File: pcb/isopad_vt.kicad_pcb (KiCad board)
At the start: 2 copper layers, 26.2 x 35.7 mm, 2 parts, among them U1 RP2040_Zero

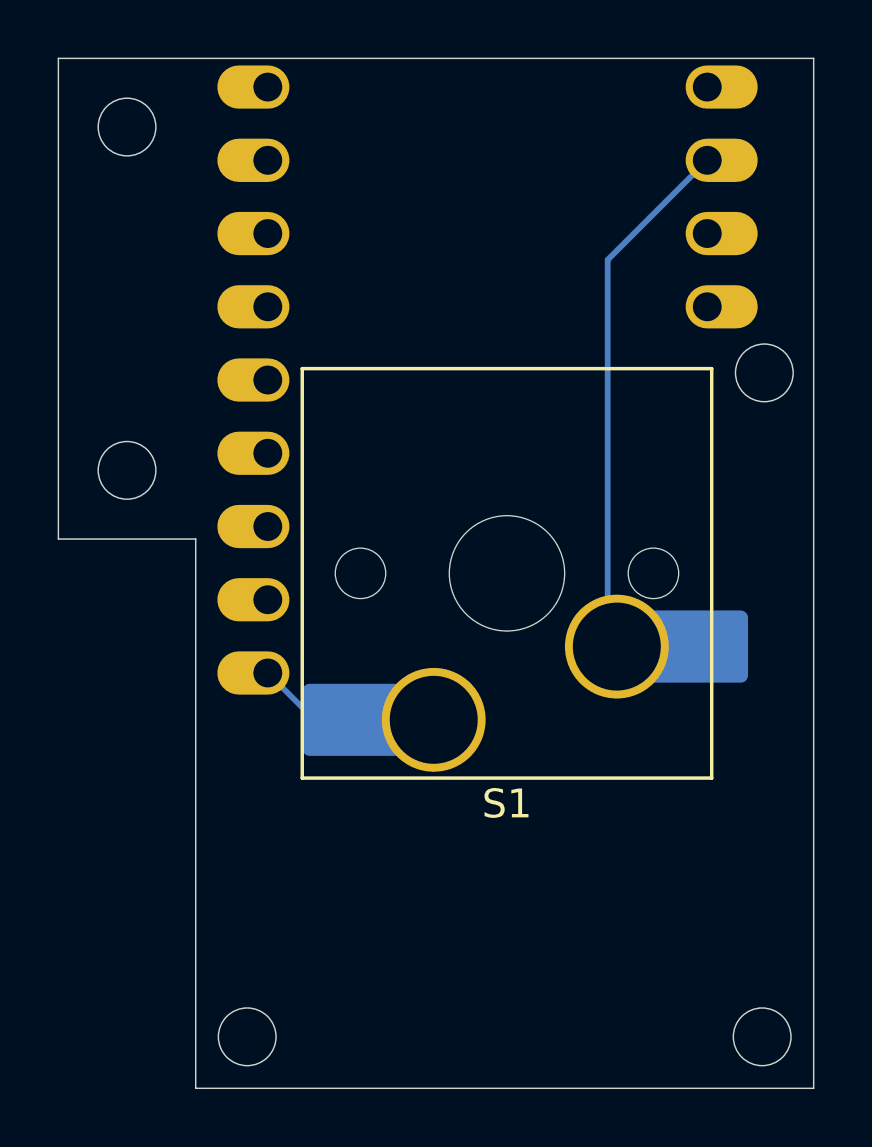
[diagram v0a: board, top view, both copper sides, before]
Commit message: case files and firmware
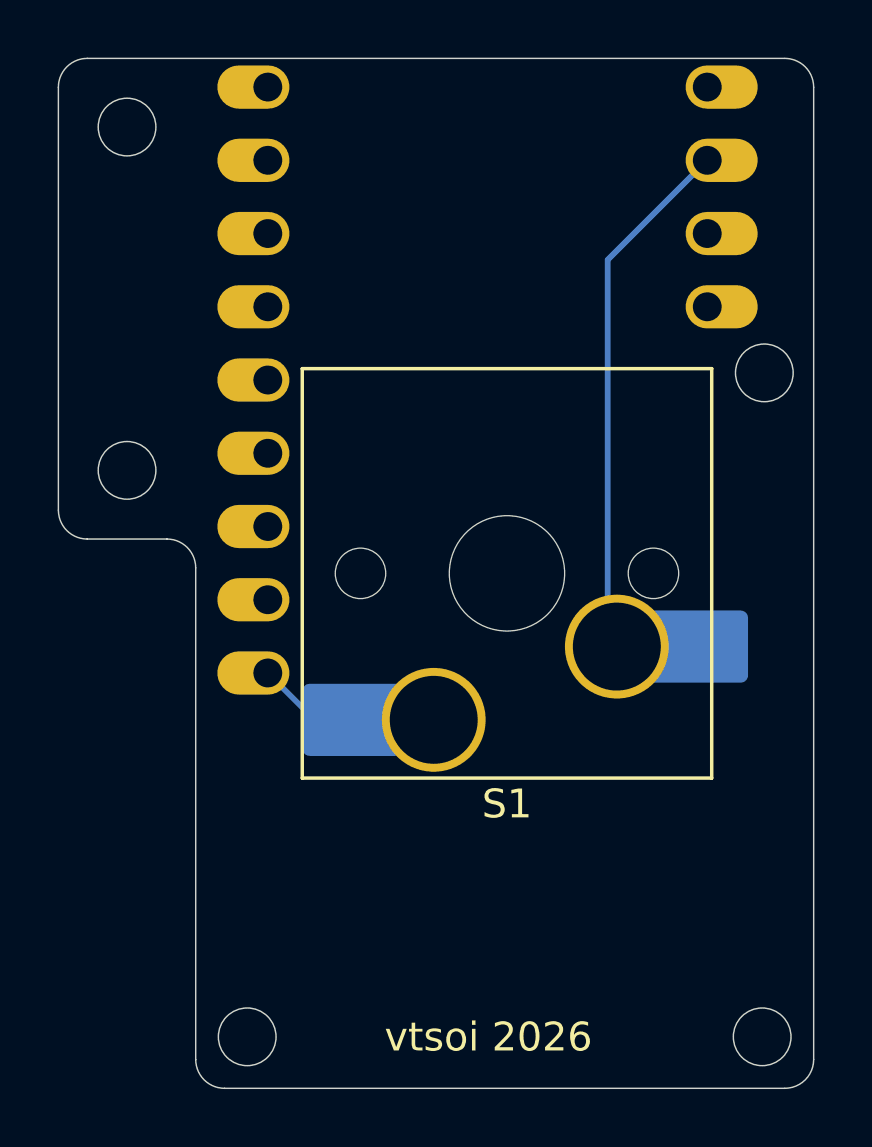
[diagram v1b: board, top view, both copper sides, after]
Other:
- outline, holes or cut-outs redrawn
- board text added: "vtsoi 2026"
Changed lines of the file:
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@@
 		(tags "Kailh Keyboard Keyswitch Switch Hotswap Socket Plated Relief Cutout Keycap ISOEnter 180deg")
 		(property "Reference" "S1"
-			(at 0 -8 360)
+			(at 0 -8 0)
 			(layer "F.SilkS")
 			(effects
@@
 		)
 		(property "Value" "Keyswitch"
-			(at 0 8 360)
+			(at 0 8 0)
 			(layer "F.Fab")
 			(effects
@@
 		)
 		(property "Footprint" "PCM_Switch_Keyboard_Hotswap_Kailh:SW_Hotswap_Kailh_MX_Plated_ISOEnter_180deg"
-			(at 0 0 360)
+			(at 0 0 0)
 			(layer "F.Fab")
 			(hide yes)
@@
 		)
 		(property "Datasheet" ""
-			(at 0 0 360)
+			(at 0 0 0)
 			(layer "F.Fab")
 			(hide yes)
@@
 		)
 		(property "Description" "Push button switch, normally open, two pins, 45° tilted"
-			(at 0 0 360)
+			(at 0 0 0)
 			(layer "F.Fab")
 			(hide yes)
@@
 		)
 		(fp_text user "${REFERENCE}"
-			(at 0 0 360)
+			(at 0 0 0)
 			(layer "F.Fab")
 			(effects
@@
 	)
 	(gr_line
-		(start 134.540625 72.628125)
-		(end 139.303125 72.628125)
+		(start 135.540625 72.628125)
+		(end 138.303125 72.628125)
 		(stroke
 			(width 0.05)
@@
 		(layer "Edge.Cuts")
 	)
+	(gr_arc
+		(start 140.303125 91.678125)
+		(mid 139.596018 91.385232)
+		(end 139.303125 90.678125)
+		(stroke
+			(width 0.05)
+			(type default)
+		)
+		(layer "Edge.Cuts")
+	)
+	(gr_arc
+		(start 160.734375 90.678125)
+		(mid 160.441471 91.385207)
+		(end 159.734375 91.678125)
+		(stroke
+			(width 0.05)
+			(type default)
+		)
+		(layer "Edge.Cuts")
+	)
 	(gr_line
-		(start 134.540625 55.959375)
-		(end 134.540625 72.628125)
+		(start 134.540625 56.959375)
+		(end 134.540625 71.628125)
 		(stroke
 			(width 0.05)
@@
 	)
 	(gr_line
-		(start 139.303125 91.678125)
-		(end 160.734375 91.678125)
+		(start 140.303125 91.678125)
+		(end 159.734375 91.678125)
+		(stroke
+			(width 0.05)
+			(type default)
+		)
+		(layer "Edge.Cuts")
+	)
+	(gr_arc
+		(start 159.734375 55.959375)
+		(mid 160.441482 56.252268)
+		(end 160.734375 56.959375)
+		(stroke
+			(width 0.05)
+			(type default)
+		)
+		(layer "Edge.Cuts")
+	)
+	(gr_arc
+		(start 134.540625 56.959375)
+		(mid 134.833518 56.252268)
+		(end 135.540625 55.959375)
 		(stroke
 			(width 0.05)
@@
 	)
 	(gr_line
-		(start 160.734375 55.959375)
-		(end 134.540625 55.959375)
+		(start 159.734375 55.959375)
+		(end 135.540625 55.959375)
 		(stroke
 			(width 0.05)
@@
 		(layer "Edge.Cuts")
 	)
+	(gr_arc
+		(start 138.303125 72.628125)
+		(mid 139.010232 72.921018)
+		(end 139.303125 73.628125)
+		(stroke
+			(width 0.05)
+			(type default)
+		)
+		(layer "Edge.Cuts")
+	)
 	(gr_circle
 		(center 136.921875 70.246875)
@@
 		(layer "Edge.Cuts")
 	)
+	(gr_arc
+		(start 135.540625 72.628125)
+		(mid 134.833518 72.335232)
+		(end 134.540625 71.628125)
+		(stroke
+			(width 0.05)
+			(type default)
+		)
+		(layer "Edge.Cuts")
+	)
 	(gr_circle
 		(center 136.921875 58.340625)
@@
 	)
 	(gr_line
-		(start 139.303125 72.628125)
-		(end 139.303125 91.678125)
+		(start 139.303125 73.628125)
+		(end 139.303125 90.678125)
 		(stroke
 			(width 0.05)
@@
 	)
 	(gr_line
-		(start 160.734375 91.678125)
-		(end 160.734375 55.959375)
-		(stroke
-			(width 0.05)
-			(type default)
-		)
-		(layer "Edge.Cuts")
+		(start 160.734375 90.678125)
+		(end 160.734375 56.959375)
+		(stroke
+			(width 0.05)
+			(type default)
+		)
+		(layer "Edge.Cuts")
+	)
+	(gr_text "vtsoi 2026"
+		(at 145.851685 90.487576 0)
+		(layer "F.SilkS")
+		(effects
+			(font
+				(size 1 1)
+				(thickness 0.1)
+			)
+			(justify left bottom)
+		)
 	)
 	(segment
